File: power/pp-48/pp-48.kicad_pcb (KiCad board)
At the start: 4 copper layers, 50 x 72 mm, 110 parts, among them J101 NODE 19V, J102 FRONT PANEL, J103 AUX, J201 NODE 19V, J202 FRONT PANEL, J203 AUX, Q101 BSC070N10NS5, Q102 2N7002, Q103 2N7002, Q104 2N7002, Q105 2N7002, Q201 BSC070N10NS5, Q202 2N7002, Q203 2N7002, Q204 2N7002, Q205 2N7002, U101 LM5069MM-2, U102 INA238AIDGSR, U103 74LVC1G74, U104 ADC121C027CIMK, U105 TCA9535PWR, U106 TLP176AM, U107 TLP176AM, U108 TLP291, U201 LM5069MM-2, U202 INA238AIDGSR, U203 74LVC1G74, U204 ADC121C027CIMK, U205 TCA9535PWR, U206 TLP176AM, U207 TLP176AM, U208 TLP291

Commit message: pp-48: slot OVLO 124k / 4.99k (64.6 V, 60.9-68.5 V worst case, below the module's 67.5 V nominally); D1 SMBJ60A kept (breakdown >= 66.7 V, SMBJ64A clamps at 103 V); values synced to the board, DRC unchanged; ADR 0003 items closed
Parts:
- R105, R205: value 240k -> 124k
- R106, R206: value 10k -> 4.99k
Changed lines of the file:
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@@
 			)
 		)
-		(property "Value" "240k"
+		(property "Value" "124k"
 			(at 0 1.65 90)
 			(layer "F.Fab")
@@
 			)
 		)
-		(property "Description" "OVLO: off 62.5 V, back at 57.5 V (to raise to ~66-68 V, ADR 0003)"
+		(property "Description" "OVLO: off 64.6 V (60.9-68.5 V over 2.4-2.6 V and 1 %), back on ~2.6 V lower (12-30 uA x 124k); module trips at 67.5 V"
 			(at 0 0 90)
 			(layer "F.Fab")
@@
 			)
 		)
-		(property "Value" "10k"
+		(property "Value" "4.99k"
 			(at 0 1.17 90)
 			(layer "F.Fab")
@@
 			)
 		)
-		(property "LCSC" "C25744"
+		(property "LCSC" ""
 			(at 0 0 90)
 			(layer "F.Fab")
@@
 			)
 		)
-		(property "Value" "240k"
+		(property "Value" "124k"
 			(at 0 1.65 90)
 			(layer "F.Fab")
@@
 			)
 		)
-		(property "Description" "OVLO: off 62.5 V, back at 57.5 V (to raise to ~66-68 V, ADR 0003)"
+		(property "Description" "OVLO: off 64.6 V (60.9-68.5 V over 2.4-2.6 V and 1 %), back on ~2.6 V lower (12-30 uA x 124k); module trips at 67.5 V"
 			(at 0 0 90)
 			(layer "F.Fab")
@@
 			)
 		)
-		(property "Value" "10k"
+		(property "Value" "4.99k"
 			(at 0 1.17 90)
 			(layer "F.Fab")
@@
 			)
 		)
-		(property "LCSC" "C25744"
+		(property "LCSC" ""
 			(at 0 0 90)
 			(layer "F.Fab")
@@
 			)
 		)
-		(property "Description" "slot output clamp (cable inductance on a cut); 60 V standoff vs the 60 V top of range: open"
+		(property "Description" "slot output clamp: 60 V standoff = top of the bus range, breakdown >= 66.7 V; SMBJ64A would clamp at 103 V, over the 100 V FET and module"
 			(at 0 0 180)
 			(unlocked yes)
@@
 			)
 		)
-		(property "Description" "slot output clamp (cable inductance on a cut); 60 V standoff vs the 60 V top of range: open"
+		(property "Description" "slot output clamp: 60 V standoff = top of the bus range, breakdown >= 66.7 V; SMBJ64A would clamp at 103 V, over the 100 V FET and module"
 			(at 0 0 180)
 			(unlocked yes)

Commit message: pp-48: slot latch also set by the INA238 ALERT (straight onto OVK, R25 gone) and by PGOOD loss with arm-on-first-PGOOD blanking (U10 set while PG and PGD high via Q8 / Q9, cleared while PGD low; trip FET Q6; DISARM on expander P10 via Q7 around RUNOFF); arm cluster on F at the left edge, U3 OVK / CLRN escape vias in route_hand.py; column 1 rerouted and copied, solid GND on starved pads, silk; DRC 5 excluded core-side ends (exclusions re-keyed), 0 unconnected, 0 parity; ADR 0003 items closed, handoff
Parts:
- removed R125, R225: 10k, Resistor_SMD:R_0402_1005Metric
- added C112: 100n, Capacitor_SMD:C_0402_1005Metric, F.Cu at (105.6, 125.6)
- added C212: 100n, Capacitor_SMD:C_0402_1005Metric, F.Cu at (130.6, 125.6)
- added Q106: 2N7002, Package_TO_SOT_SMD:SOT-23, B.Cu at (117.0, 140.5)
- added Q107: 2N7002, Package_TO_SOT_SMD:SOT-23, F.Cu at (102.6, 121.8)
- added Q108: 2N7002, Package_TO_SOT_SMD:SOT-23, F.Cu at (102.4, 129.8)
- added Q109: 2N7002, Package_TO_SOT_SMD:SOT-23, F.Cu at (106.6, 129.8)
- added Q206: 2N7002, Package_TO_SOT_SMD:SOT-23, B.Cu at (142.0, 140.5)
- added Q207: 2N7002, Package_TO_SOT_SMD:SOT-23, F.Cu at (127.6, 121.8)
- added Q208: 2N7002, Package_TO_SOT_SMD:SOT-23, F.Cu at (127.4, 129.8)
- added Q209: 2N7002, Package_TO_SOT_SMD:SOT-23, F.Cu at (131.6, 129.8)
- added R128: 100k, Resistor_SMD:R_0402_1005Metric, F.Cu at (107.6, 125.6)
- added R129: 100k, Resistor_SMD:R_0402_1005Metric, F.Cu at (105.6, 121.8)
- added R228: 100k, Resistor_SMD:R_0402_1005Metric, F.Cu at (132.6, 125.6)
- added R229: 100k, Resistor_SMD:R_0402_1005Metric, F.Cu at (130.6, 121.8)
- added U110: 74LVC1G74, Package_SO:VSSOP-8_2.3x2mm_P0.5mm, F.Cu at (102.8, 125.6)
- added U210: 74LVC1G74, Package_SO:VSSOP-8_2.3x2mm_P0.5mm, F.Cu at (127.8, 125.6)
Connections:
- U102 pad 3: /Column 1/INA_AL -> /Column 1/OVK
- U105 pad 13: unconnected-(U105-P10-Pad13) -> /Column 1/DISARM
- U105 pad 4: /Column 1/INA_AL -> unconnected-(U105-P00-Pad4)
- U202 pad 3: /Column 2/INA_AL -> /Column 2/OVK
- U205 pad 13: unconnected-(U205-P10-Pad13) -> /Column 2/DISARM
- U205 pad 4: /Column 2/INA_AL -> unconnected-(U205-P00-Pad4)
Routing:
- net GND: track 67.7 -> 134.3 mm, vias 30 -> 36
- net /Column 2/PG: track 13.2 -> 78.3 mm, vias 2 -> 11
- net /Column 1/PG: track 13.2 -> 78.3 mm, vias 2 -> 11
- net /Column 1/OVK: track 21.5 -> 63.3 mm, vias 2 -> 6
- net /Column 2/OVK: track 21.5 -> 63.3 mm, vias 2 -> 6
- net /Column 1/INA_AL: track 37.0 -> 0.00 mm, vias 2 -> 0
- net /Column 2/INA_AL: track 37.0 -> 0.00 mm, vias 2 -> 0
- net /Column 2/PGD: track 22.1 -> 48.0 mm, vias 2 -> 4
- net /Column 1/PGD: track 22.1 -> 48.0 mm, vias 2 -> 4
- net /Column 1/DISARM: track 0.00 -> 25.8 mm, vias 0 -> 3
- net /Column 2/DISARM: track 0.00 -> 25.8 mm, vias 0 -> 3
- net /Column 2/ARM: track 0.00 -> 23.6 mm, vias 0 -> 1
- net /Column 1/ARM: track 0.00 -> 23.6 mm, vias 0 -> 1
- net /Column 2/ARMS_N: track 0.00 -> 13.5 mm, vias 0 -> 2
- net /Column 1/ARMS_N: track 0.00 -> 13.5 mm, vias 0 -> 2
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
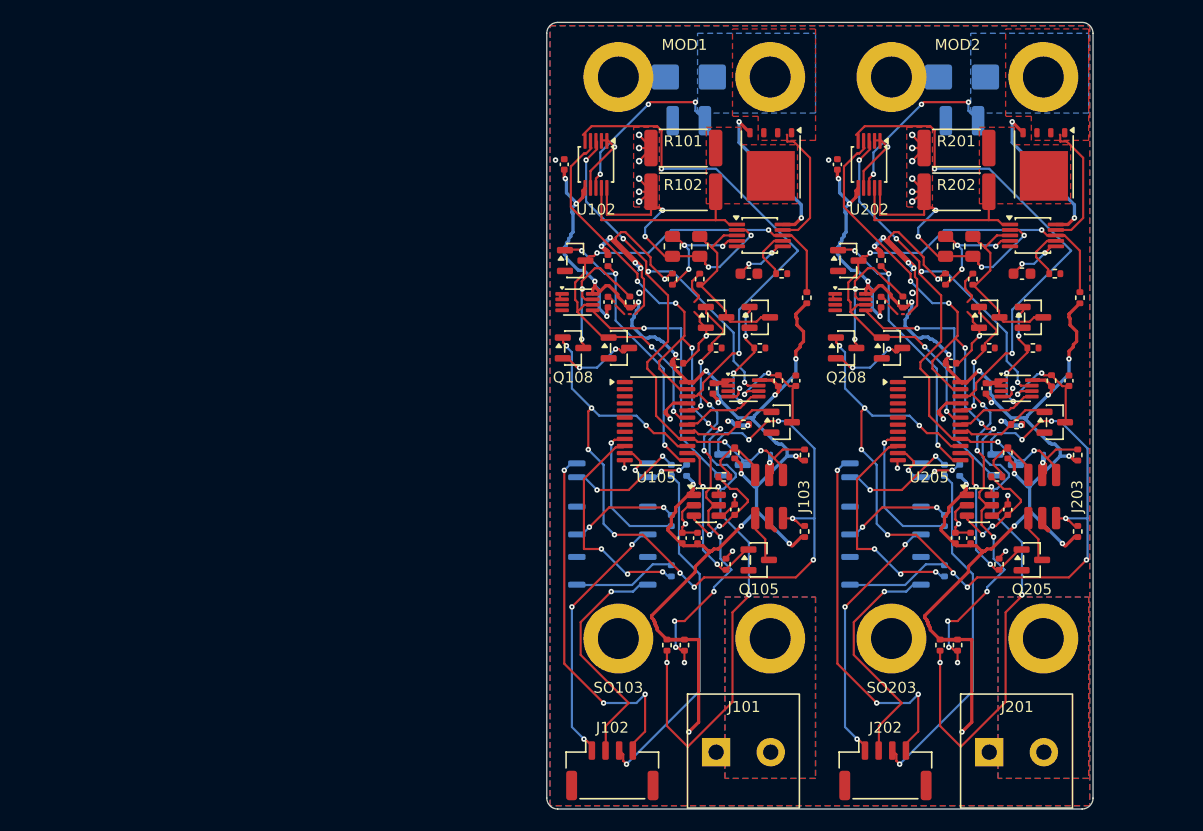
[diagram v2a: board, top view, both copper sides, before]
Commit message: pp-48: board routed with the core (N = 2, 106 x 72): DRC 0 unconnected / 0 parity / 0 errors, old track_dangling exclusions gone; route_hand.py core(): tile VIN / TSENSE / VBUS copper, Kelvin sense for U7 / U8, In2 channel rows under the VBUS via field to a via ladder and the mux, +3V3 trunk end, CTRL_GND pours with a 2 mm isolation band; tools/netsplit.py renames +3V3 and COLn per column around krt-route (KRT does not count In2 tracks as connections); gndstitch also stitches CTRL_GND; copycol keeps the core routes; placement changes in core.py; J1 retention pegs on GND; core channel limited to N <= 4
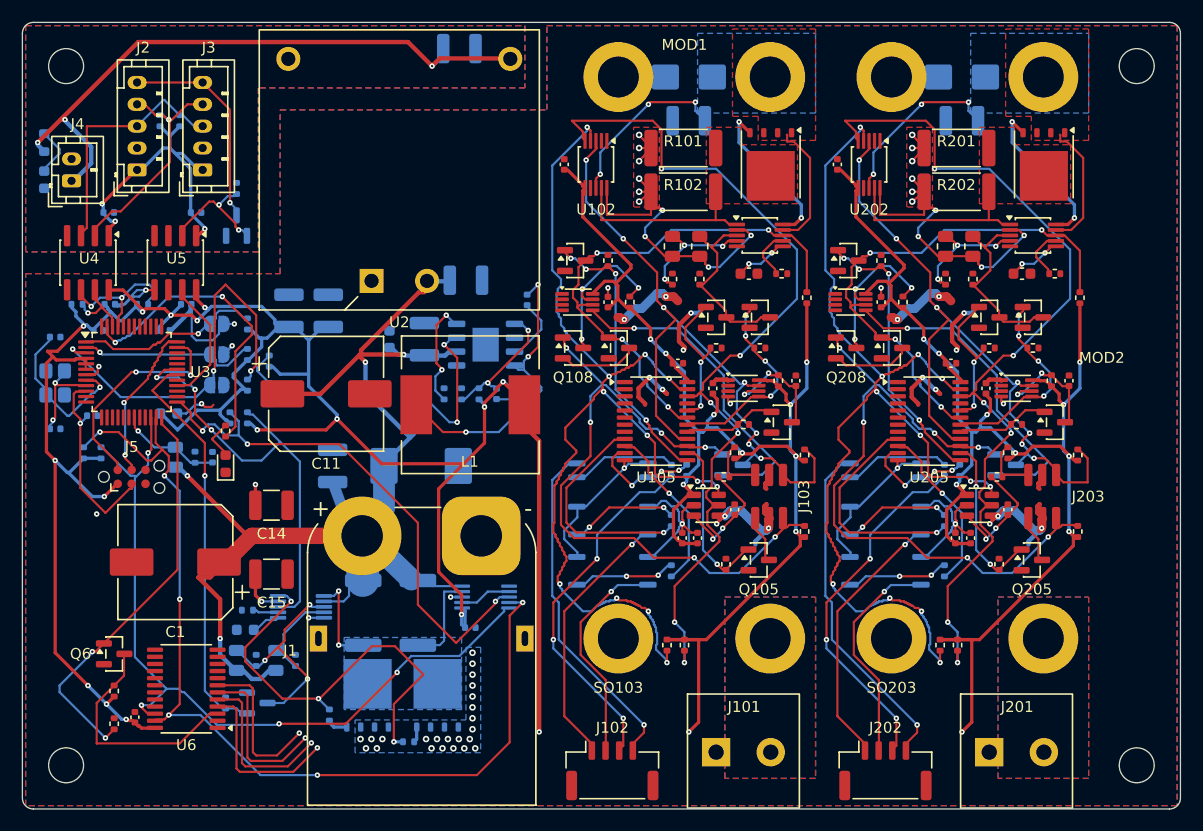
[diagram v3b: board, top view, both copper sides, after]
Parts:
- added C1: 47u 100V, Capacitor_SMD:CP_Elec_10x10, F.Cu at (66.0, 149.4)
- added C10: 22u 10V, Capacitor_SMD:C_1210_3225Metric, B.Cu at (80.0, 126.4)
- added C11: 22u 100V, Capacitor_SMD:CP_Elec_10x10, F.Cu at (79.8, 134.0)
- added C12: 2.2u 100V, Capacitor_SMD:C_1210_3225Metric, B.Cu at (92.6, 123.6)
- added C13: 10u 50V, Capacitor_SMD:C_1210_3225Metric, B.Cu at (92.0, 102.4)
- added C14: 2.2u 100V, Capacitor_SMD:C_1210_3225Metric, F.Cu at (74.8, 144.2)
- added C15: 2.2u 100V, Capacitor_SMD:C_1210_3225Metric, F.Cu at (74.8, 150.5)
- added C16: 100n, Capacitor_SMD:C_0402_1005Metric, B.Cu at (93.0, 155.4)
- added C17: 100n, Capacitor_SMD:C_0402_1005Metric, B.Cu at (69.4, 139.8)
- added C18: 100n, Capacitor_SMD:C_0402_1005Metric, B.Cu at (59.0, 128.2)
- added C19: 4.7u, Capacitor_SMD:C_0603_1608Metric, B.Cu at (65.4, 135.8)
- added C2: 2.2u 100V, Capacitor_SMD:C_1210_3225Metric, B.Cu at (80.4, 140.6)
- added C20: 100n, Capacitor_SMD:C_0402_1005Metric, B.Cu at (65.0, 128.2)
- added C21: 100n, Capacitor_SMD:C_0402_1005Metric, B.Cu at (58.4, 136.0)
- added C22: 33p, Capacitor_SMD:C_0402_1005Metric, B.Cu at (55.0, 128.8)
- added C23: 33p, Capacitor_SMD:C_0402_1005Metric, B.Cu at (55.0, 137.2)
- added C24: 100n, Capacitor_SMD:C_0402_1005Metric, B.Cu at (59.9, 117.4)
- added C25: 100n, Capacitor_SMD:C_0402_1005Metric, B.Cu at (60.0, 125.8)
- added C26: 100n, Capacitor_SMD:C_0402_1005Metric, B.Cu at (67.9, 117.4)
- added C27: 100n, Capacitor_SMD:C_0402_1005Metric, B.Cu at (67.0, 125.8)
- added C28: 100n, Capacitor_SMD:C_0402_1005Metric, F.Cu at (62.3, 163.6)
- added C3: 220n, Capacitor_SMD:C_0603_1608Metric, B.Cu at (72.4, 155.6)
- added C4: 2.2n 50V, Capacitor_SMD:C_0402_1005Metric, B.Cu at (98.2, 125.4)
- added C5: 1.5n, Capacitor_SMD:C_0402_1005Metric, B.Cu at (97.0, 134.0)
- added C6: 100n, Capacitor_SMD:C_0402_1005Metric, B.Cu at (95.4, 134.0)
- added C7: 2.2u 100V, Capacitor_SMD:C_1210_3225Metric, B.Cu at (88.8, 129.0)
- added C8: 100n 100V, Capacitor_SMD:C_0603_1608Metric, B.Cu at (85.6, 129.0)
- added C9: 22u 10V, Capacitor_SMD:C_1210_3225Metric, B.Cu at (76.4, 126.4)
- added D1: SMDJ60A, Diode_SMD:D_SMC, B.Cu at (88.5, 140.6)
- added D3: GREEN 3V3, LED_SMD:LED_0603_1608Metric, B.Cu at (74.6, 134.0)
- added D4: GREEN RUN, LED_SMD:LED_0603_1608Metric, F.Cu at (70.6, 140.4)
- added D5: GREEN 12V, LED_SMD:LED_0603_1608Metric, B.Cu at (54.0, 114.4)
- added H1: MountingHole_3.2mm_M3, MountingHole:MountingHole_3.2mm_M3, F.Cu at (56.0, 104.0)
- added H2: MountingHole_3.2mm_M3, MountingHole:MountingHole_3.2mm_M3, F.Cu at (154.0, 104.0)
- added H3: MountingHole_3.2mm_M3, MountingHole:MountingHole_3.2mm_M3, F.Cu at (154.0, 168.0)
- added H4: MountingHole_3.2mm_M3, MountingHole:MountingHole_3.2mm_M3, F.Cu at (56.0, 168.0)
- added J1: XT90PW-M, Connector_AMASS:AMASS_XT90PW-M_1x02_P10.90mm_Horizontal, F.Cu at (94.0, 147.0)
- added J2: CTRL IN, Connector_JST:JST_PH_B5B-PH-K_1x05_P2.00mm_Vertical, F.Cu at (62.5, 113.5)
- added J3: CTRL OUT, Connector_JST:JST_PH_B5B-PH-K_1x05_P2.00mm_Vertical, F.Cu at (68.5, 113.5)
- added J4: 12V AUX OUT, Connector_JST:JST_PH_B2B-PH-K_1x02_P2.00mm_Vertical, F.Cu at (56.5, 114.5)
- added J5: SWD, Connector:Tag-Connect_TC2030-IDC-NL_2x03_P1.27mm_Vertical, F.Cu at (62.0, 141.6)
- added JP1: ADR0, Jumper:SolderJumper-2_P1.3mm_Open_RoundedPad1.0x1.5mm, B.Cu at (69.8, 127.6)
- added JP2: ADR1, Jumper:SolderJumper-2_P1.3mm_Open_RoundedPad1.0x1.5mm, B.Cu at (69.8, 130.4)
- added JP3: ADR2, Jumper:SolderJumper-2_P1.3mm_Open_RoundedPad1.0x1.5mm, B.Cu at (69.8, 133.2)
- added L1: 33u, Inductor_SMD:L_12x12mm_H6mm, F.Cu at (93.0, 135.0)
- added Q1: 2N7002, Package_TO_SOT_SMD:SOT-23, B.Cu at (71.6, 118.6)
- added Q2: BSC040N10NS5, Package_TO_SOT_SMD:TDSON-8-1, B.Cu at (83.6, 161.6)
- added Q3: BSC040N10NS5, Package_TO_SOT_SMD:TDSON-8-1, B.Cu at (90.0, 161.6)
- added Q4: 2N7002, Package_TO_SOT_SMD:SOT-23, B.Cu at (73.5, 162.3)
- added Q6: 2N7002, Package_TO_SOT_SMD:SOT-23, F.Cu at (60.4, 157.8)
- added R1: 4m 2W, Resistor_SMD:R_2512_6332Metric, B.Cu at (83.2, 154.1)
- added R10: 10, Resistor_SMD:R_0402_1005Metric, B.Cu at (80.1, 163.4)
- added R11: 10, Resistor_SMD:R_0402_1005Metric, B.Cu at (87.3, 165.8)
- added R12: 10k, Resistor_SMD:R_0402_1005Metric, B.Cu at (71.0, 136.2)
- added R14: 100k, Resistor_SMD:R_0402_1005Metric, B.Cu at (70.6, 162.3)
- added R15: 220k, Resistor_SMD:R_0805_2012Metric, B.Cu at (66.0, 139.8)
- added R16: 10k, Resistor_SMD:R_0402_1005Metric, B.Cu at (67.8, 139.8)
- added R18: 1k, Resistor_SMD:R_0402_1005Metric, B.Cu at (74.6, 131.0)
- added R19: 1k, Resistor_SMD:R_0402_1005Metric, F.Cu at (70.6, 137.4)
- added R2: 4m 2W, Resistor_SMD:R_2512_6332Metric, B.Cu at (88.2, 154.1)
- added R20: 100k, Resistor_SMD:R_0402_1005Metric, B.Cu at (72.6, 127.6)
- added R21: 100k, Resistor_SMD:R_0402_1005Metric, B.Cu at (72.6, 130.4)
- added R22: 100k, Resistor_SMD:R_0402_1005Metric, B.Cu at (72.6, 133.2)
- added R23: 2.2k, Resistor_SMD:R_0402_1005Metric, B.Cu at (57.6, 139.4)
- added R24: 2.2k, Resistor_SMD:R_0402_1005Metric, B.Cu at (59.2, 139.4)
- added R26: 4.7k, Resistor_SMD:R_0402_1005Metric, B.Cu at (57.0, 125.8)
- added R27: 4.7k, Resistor_SMD:R_0402_1005Metric, B.Cu at (63.0, 125.8)
- added R28: 4.7k, Resistor_SMD:R_0402_1005Metric, B.Cu at (64.6, 109.0)
- added R29: 4.7k, Resistor_SMD:R_0402_1005Metric, B.Cu at (66.4, 109.0)
- added R3: 1M, Resistor_SMD:R_0805_2012Metric, B.Cu at (87.4, 134.0)
- added R30: 100k, Resistor_SMD:R_0402_1005Metric, B.Cu at (71.6, 115.2)
- added R31: 10k, Resistor_SMD:R_0402_1005Metric, F.Cu at (60.4, 161.2)
- added R32: 100k, Resistor_SMD:R_0402_1005Metric, F.Cu at (60.4, 164.2)
- added R33: 143k, Resistor_SMD:R_0805_2012Metric, B.Cu at (71.6, 158.4)
- added R34: 10k, Resistor_SMD:R_0402_1005Metric, B.Cu at (73.4, 158.4)
- added R35: 124k, Resistor_SMD:R_0805_2012Metric, B.Cu at (75.2, 158.4)
- added R36: 4.99k, Resistor_SMD:R_0402_1005Metric, B.Cu at (77.0, 158.4)
- added R37: 10.2k, Resistor_SMD:R_0402_1005Metric, B.Cu at (72.6, 153.8)
- added R38: 10k, Resistor_SMD:R_0402_1005Metric, B.Cu at (72.6, 136.2)
- added R4: 52.3k, Resistor_SMD:R_0402_1005Metric, B.Cu at (89.0, 134.0)
- added R5: 41.2k, Resistor_SMD:R_0402_1005Metric, B.Cu at (90.6, 134.0)
- added R6: 86.6k, Resistor_SMD:R_0402_1005Metric, B.Cu at (93.8, 134.0)
- added R7: 49.9k, Resistor_SMD:R_0402_1005Metric, B.Cu at (92.2, 134.0)
- added R8: 453k, Resistor_SMD:R_0402_1005Metric, B.Cu at (98.6, 134.0)
- added R9: 4.7k, Resistor_SMD:R_0603_1608Metric, B.Cu at (54.0, 111.0)
- added U1: LM5164DDA, Package_SO:HSOP-8-1EP_3.9x4.9mm_P1.27mm_EP2.41x3.1mm, B.Cu at (94.4, 129.5)
- added U2: URB4812YMD-6WR3, pp48:Converter_DCDC_1x1in_THT, F.Cu at (86.5, 113.5)
- added U3: STM32G070CBT6, Package_QFP:LQFP-48_7x7mm_P0.5mm, F.Cu at (62.0, 132.0)
- added U4: ISO1640BD, Package_SO:SOIC-8_3.9x4.9mm_P1.27mm, F.Cu at (58.0, 122.0)
- added U5: ISO7721D, Package_SO:SOIC-8_3.9x4.9mm_P1.27mm, F.Cu at (66.0, 122.0)
- added U6: TCA9548APWR, Package_SO:TSSOP-24_4.4x7.8mm_P0.65mm, F.Cu at (67.0, 161.0)
- added U7: LM5069MM-1, Package_SO:MSOP-10_3x3mm_P0.5mm, B.Cu at (77.5, 153.5)
- added U8: INA238AIDGSR, Package_SO:TSSOP-10_3x3mm_P0.5mm, B.Cu at (94.4, 152.6)
- added Y1: 8MHz, Crystal:Crystal_SMD_3225-4Pin_3.2x2.5mm, B.Cu at (55.0, 133.0)
- turned D101 to 180 degrees
- turned D201 to 180 degrees
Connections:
- D101 pad 1: GND -> /Column 1/OUT
- D101 pad 2: /Column 1/OUT -> GND
- D201 pad 1: GND -> /Column 2/OUT
- D201 pad 2: /Column 2/OUT -> GND
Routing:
- net +3V3: track 295.8 -> 490.8 mm, vias 32 -> 36
- net VIN: track 0.00 -> 101.8 mm, vias 0 -> 4
- net /SDA2: track 0.00 -> 88.5 mm, vias 0 -> 6
- net /SCL2: track 0.00 -> 73.0 mm, vias 0 -> 4
- net CTRL_12V: track 0.00 -> 57.7 mm, vias 0 -> 3
- net /COL2_SDA: track 122.5 -> 177.0 mm, vias 8 -> 13
- net /COL1_SDA: track 97.3 -> 150.0 mm, vias 8 -> 13
- net /COL2_SCL: track 114.3 -> 166.2 mm, vias 9 -> 7
- net /COL1_SCL: track 89.0 -> 139.2 mm, vias 9 -> 7
- net /TILE_AL: track 0.00 -> 48.5 mm, vias 0 -> 3
- net /TILE_PGD: track 0.00 -> 40.0 mm, vias 0 -> 3
- net /Input/GATE: track 0.00 -> 38.8 mm, vias 0 -> 3
- net /MUX_RST: track 0.00 -> 36.7 mm, vias 0 -> 2
- net /TILE_OFF: track 0.00 -> 36.4 mm, vias 0 -> 1
- net /MCU/ADR2: track 0.00 -> 35.4 mm, vias 0 -> 3
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- added copper zone on B.Cu, net /Input/TSENSE
- added copper zone on B.Cu, net CTRL_GND
- added copper zone on F.Cu, net CTRL_GND
- added copper zone on In1.Cu, net CTRL_GND
- added copper zone on B.Cu, net VBUS
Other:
- board size 50 x 72 mm -> 106 x 72 mm
